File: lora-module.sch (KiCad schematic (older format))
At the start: 38 parts, among them J1 SMA, P1 CONN_01X07, P2 CONN_01X07, Q1 32MHz, U2 SX1276, U5 PE4259

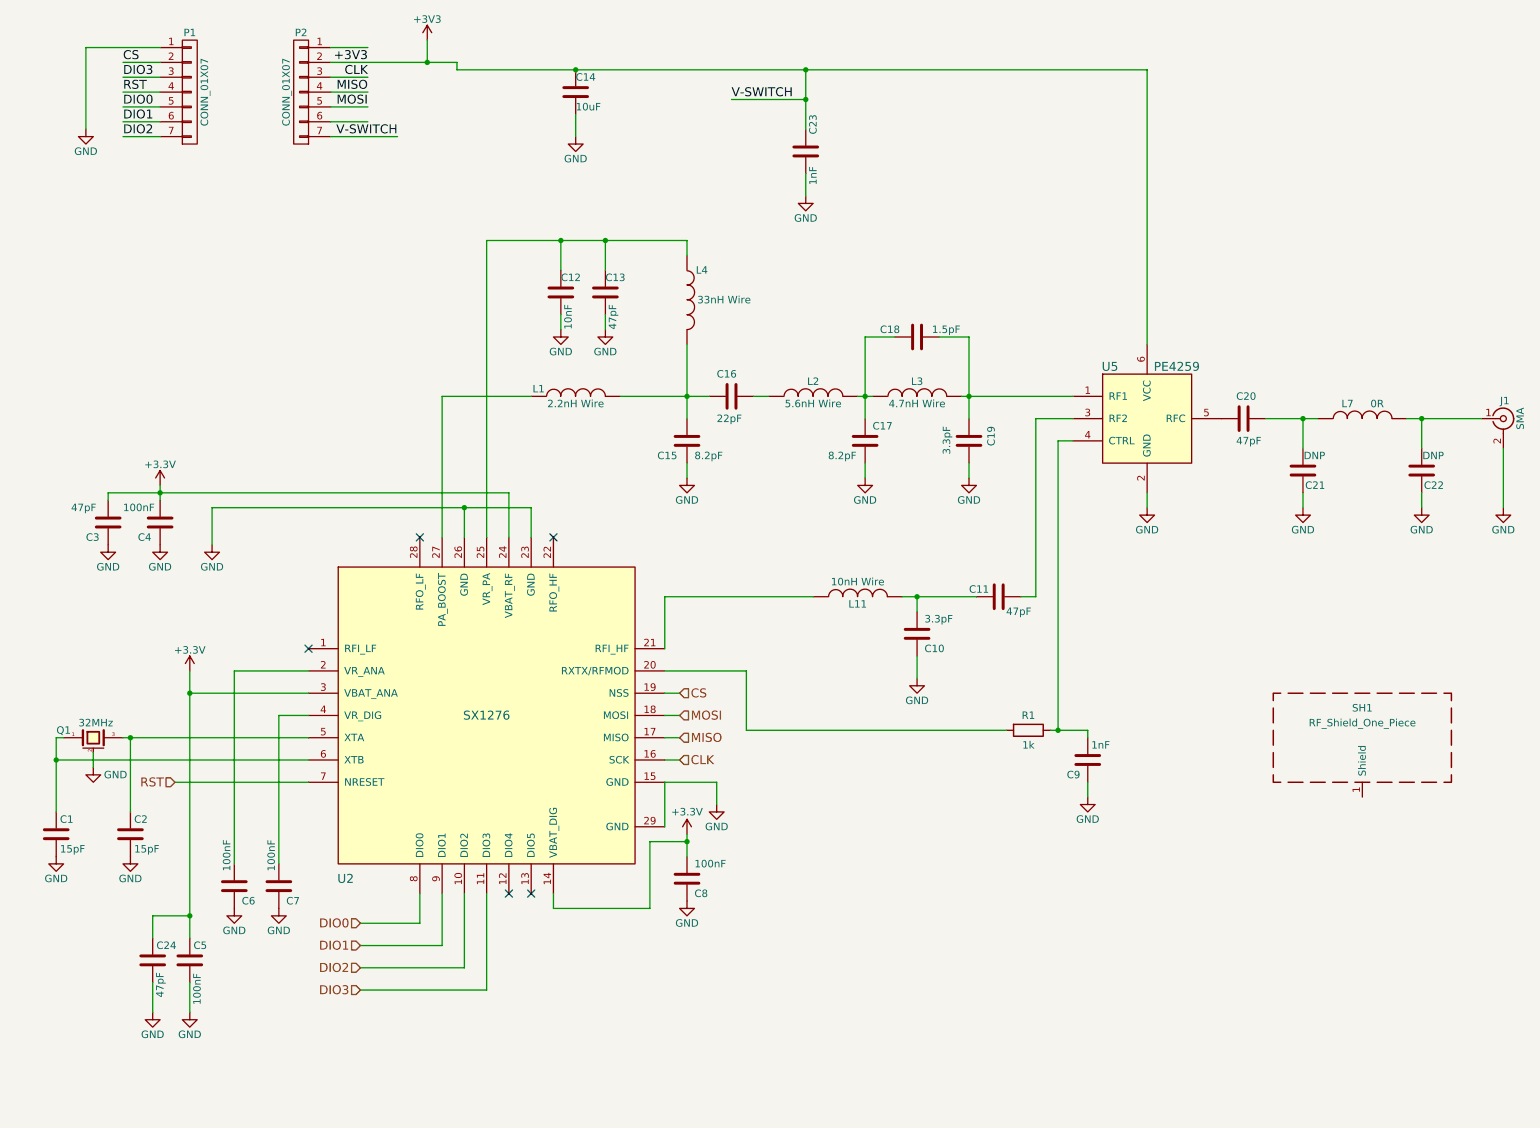
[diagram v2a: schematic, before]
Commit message: removed 2 caps, added routing
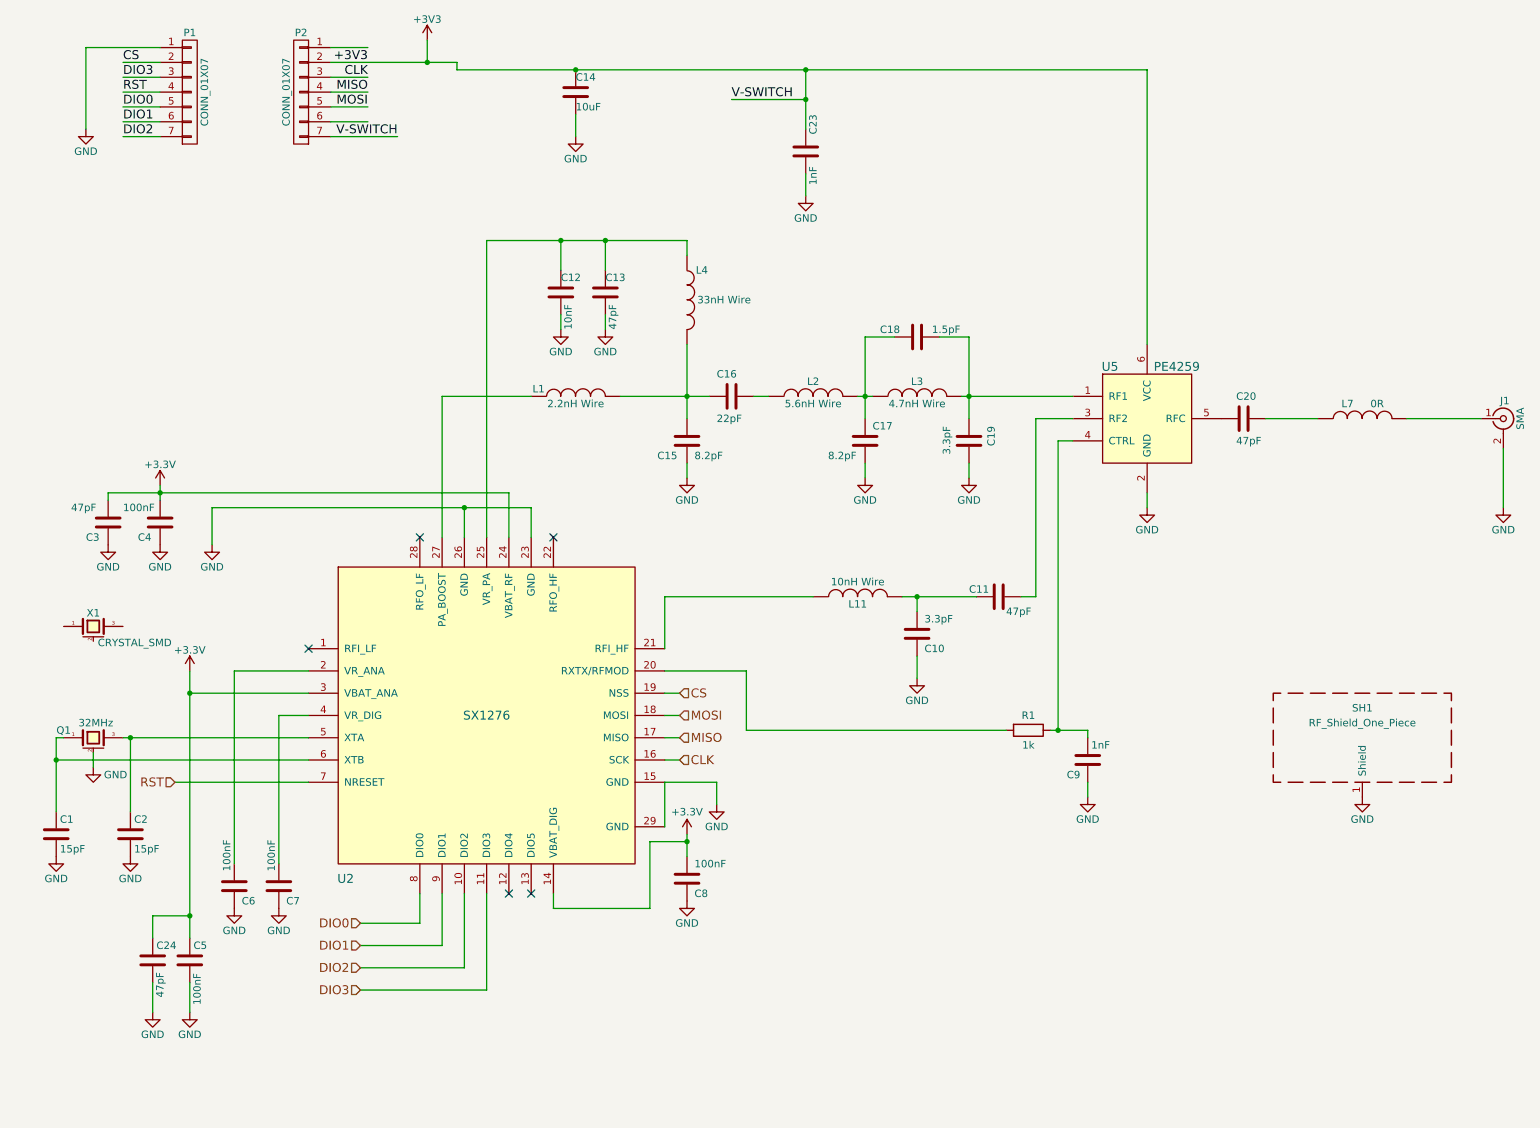
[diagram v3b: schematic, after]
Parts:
- removed C21, C22: DNP, Capacitors_SMD:C_0402, symbol C
- added X1: CRYSTAL_SMD, Crystals:Crystal_SMD_EuroQuartz_MT-4pin_3.2x2.5mm, symbol CRYSTAL_SMD
- J1: footprint (none) -> balcerzak-pcb:SMA-16
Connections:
- net GND: now also SH1.1 (Shield)
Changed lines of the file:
@@
-$EndComp
-$Comp
-L C C21
-U 1 1 59000D60
-P 9000 3650
-F 0 "C21" H 8850 3750 50  0000 L CNN
-F 1 "DNP" H 8850 3550 50  0000 L CNN
-F 2 "Capacitors_SMD:C_0402" H 9038 3500 50  0001 C CNN
-F 3 "" H 9000 3650 50  0000 C CNN
-	1    9000 3650
-	-1   0    0    1
 $EndComp
 $Comp
@@
 $EndComp
 $Comp
-L C C22
-U 1 1 590011CF
-P 9800 3650
-F 0 "C22" H 9650 3750 50  0000 L CNN
-F 1 "DNP" H 9650 3550 50  0000 L CNN
-F 2 "Capacitors_SMD:C_0402" H 9838 3500 50  0001 C CNN
-F 3 "" H 9800 3650 50  0000 C CNN
-	1    9800 3650
-	-1   0    0    1
-$EndComp
-$Comp
 L GND #PWR023
-U 1 1 59001353
-P 9000 3900
-F 0 "#PWR023" H 9000 3650 50  0001 C CNN
-F 1 "GND" H 9000 3750 50  0000 C CNN
-F 2 "" H 9000 3900 50  0000 C CNN
-F 3 "" H 9000 3900 50  0000 C CNN
-	1    9000 3900
-	1    0    0    -1
-$EndComp
-$Comp
-L GND #PWR024
-U 1 1 590013C1
-P 9800 3900
-F 0 "#PWR024" H 9800 3650 50  0001 C CNN
-F 1 "GND" H 9800 3750 50  0000 C CNN
-F 2 "" H 9800 3900 50  0000 C CNN
-F 3 "" H 9800 3900 50  0000 C CNN
-	1    9800 3900
-	1    0    0    -1
-$EndComp
-$Comp
-L GND #PWR025
 U 1 1 59026573
 P 7950 3900
-F 0 "#PWR025" H 7950 3650 50  0001 C CNN
+F 0 "#PWR023" H 7950 3650 50  0001 C CNN
 F 1 "GND" H 7950 3750 50  0000 C CNN
 F 2 "" H 7950 3900 50  0000 C CNN
@@
 	7950 3800 7950 3900
 Wire Wire Line
-	9000 3800 9000 3900
-Wire Wire Line
 	8750 3300 9100 3300
-Wire Wire Line
-	9000 3300 9000 3500
-Connection ~ 9000 3300
-Wire Wire Line
-	9800 3800 9800 3900
-Wire Wire Line
-	9800 3500 9800 3300
 Wire Wire Line
 	9700 3300 10200 3300
@@
 	800  800  800  1350
 $Comp
-L GND #PWR026
+L GND #PWR024
 U 1 1 599279CE
 P 800 1350
-F 0 "#PWR026" H 800 1100 50  0001 C CNN
+F 0 "#PWR024" H 800 1100 50  0001 C CNN
 F 1 "GND" H 800 1200 50  0000 C CNN
 F 2 "" H 800 1350 50  0001 C CNN
@@
 $EndComp
 $Comp
-L +3V3 #PWR027
+L +3V3 #PWR025
 U 1 1 599280F4
 P 3100 750
-F 0 "#PWR027" H 3100 600 50  0001 C CNN
+F 0 "#PWR025" H 3100 600 50  0001 C CNN
 F 1 "+3V3" H 3100 890 50  0000 C CNN
 F 2 "" H 3100 750 50  0001 C CNN
@@
 $EndComp
 $Comp
-L GND #PWR028
+L GND #PWR026
 U 1 1 599295F0
 P 4100 1400
-F 0 "#PWR028" H 4100 1150 50  0001 C CNN
+F 0 "#PWR026" H 4100 1150 50  0001 C CNN
 F 1 "GND" H 4100 1250 50  0000 C CNN
 F 2 "" H 4100 1400 50  0001 C CNN
@@
 Connection ~ 4100 950
 $Comp
-L GND #PWR029
+L GND #PWR027
 U 1 1 59935F61
 P 5650 1800
-F 0 "#PWR029" H 5650 1550 50  0001 C CNN
+F 0 "#PWR027" H 5650 1550 50  0001 C CNN
 F 1 "GND" H 5650 1650 50  0000 C CNN
 F 2 "" H 5650 1800 50  0001 C CNN
@@
 F 0 "J1" H 10360 3420 50  0000 C CNN
 F 1 "SMA" V 10465 3300 50  0000 C CNN
-F 2 "" H 10350 3300 50  0001 C CNN
+F 2 "balcerzak-pcb:SMA-16" H 10350 3300 50  0001 C CNN
 F 3 "" H 10350 3300 50  0001 C CNN
 	1    10350 3300
 	1    0    0    -1
 $EndComp
-Connection ~ 9800 3300
-$Comp
-L GND #PWR030
+$Comp
+L GND #PWR028
 U 1 1 59CF457A
 P 10350 3900
-F 0 "#PWR030" H 10350 3650 50  0001 C CNN
+F 0 "#PWR028" H 10350 3650 50  0001 C CNN
 F 1 "GND" H 10350 3750 50  0000 C CNN
 F 2 "" H 10350 3900 50  0000 C CNN
@@
 Wire Wire Line
 	10350 3500 10350 3900
+$Comp
+L CRYSTAL_SMD X1
+U 1 1 59D13E04
+P 850 4700
+F 0 "X1" H 850 4790 50  0000 C CNN
+F 1 "CRYSTAL_SMD" H 880 4590 50  0000 L CNN
+F 2 "Crystals:Crystal_SMD_EuroQuartz_MT-4pin_3.2x2.5mm" H 850 4700 50  0001 C CNN
+F 3 "" H 850 4700 50  0000 C CNN
+	1    850  4700
+	1    0    0    -1
+$EndComp
+$Comp
+L GND #PWR?
+U 1 1 59D14F41
+P 9400 5850
+F 0 "#PWR?" H 9400 5600 50  0001 C CNN
+F 1 "GND" H 9400 5700 50  0000 C CNN
+F 2 "" H 9400 5850 50  0001 C CNN
+F 3 "" H 9400 5850 50  0001 C CNN
+	1    9400 5850
+	1    0    0    -1
+$EndComp
 $EndSCHEMATC

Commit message: schematic simplified
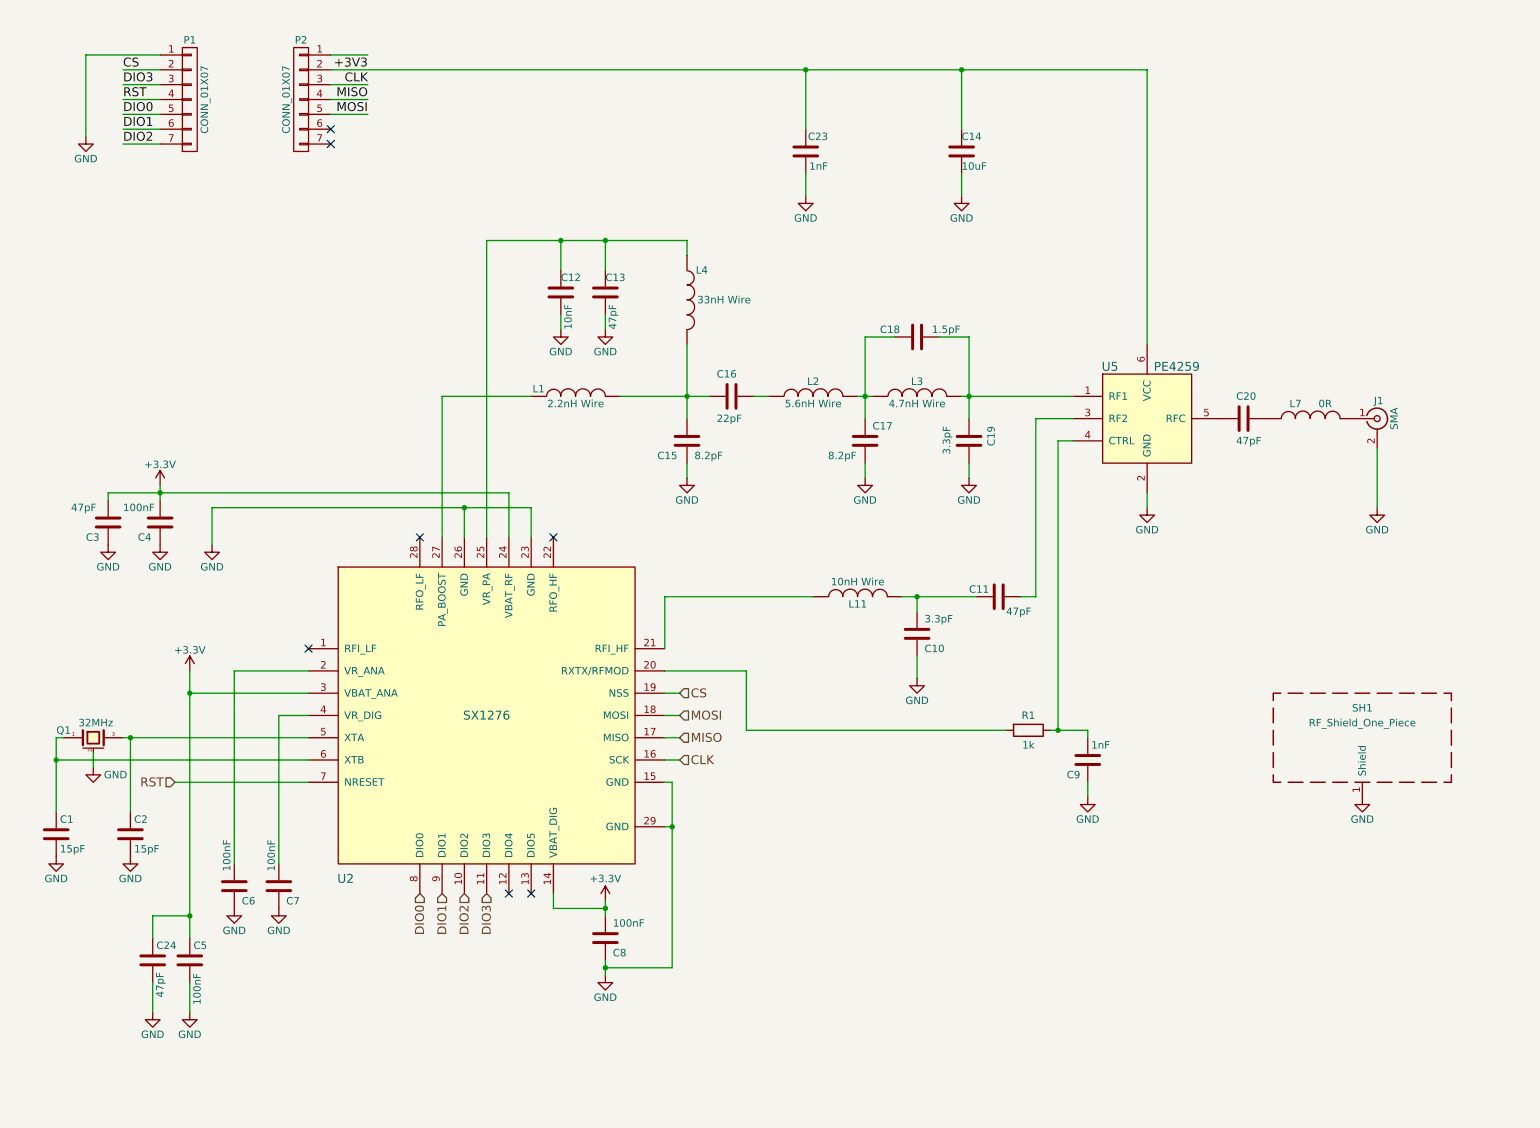
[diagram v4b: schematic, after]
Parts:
- removed X1: CRYSTAL_SMD, Crystals:Crystal_SMD_EuroQuartz_MT-4pin_3.2x2.5mm, symbol CRYSTAL_SMD
- U5: footprint TO_SOT_Packages_SMD:SOT-363_SC-70-6 -> balcerzak-pcb:SOT-363_SC-70-6
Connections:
- net +3V3: no longer P2.7 (P7)
- no-connect marks 5 -> 7
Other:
- moved on the sheet: C14, C8, J1, L7, P1, P2
